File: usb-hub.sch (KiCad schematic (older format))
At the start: 51 parts, among them J1 USB_C_Receptacle_16pin, J2 USB_C_Receptacle_16pin, J3 USB_C_Receptacle_16pin, J4 Conn_01x01_Female, J5 Conn_01x01_Female, J6 Conn_01x01_Female, J7 Conn_01x01_Female, P1 CONN_02X03, Q1 PMOS, -3.6A, 0.02R, Q2 Q_NMOS_GSD 1Amp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

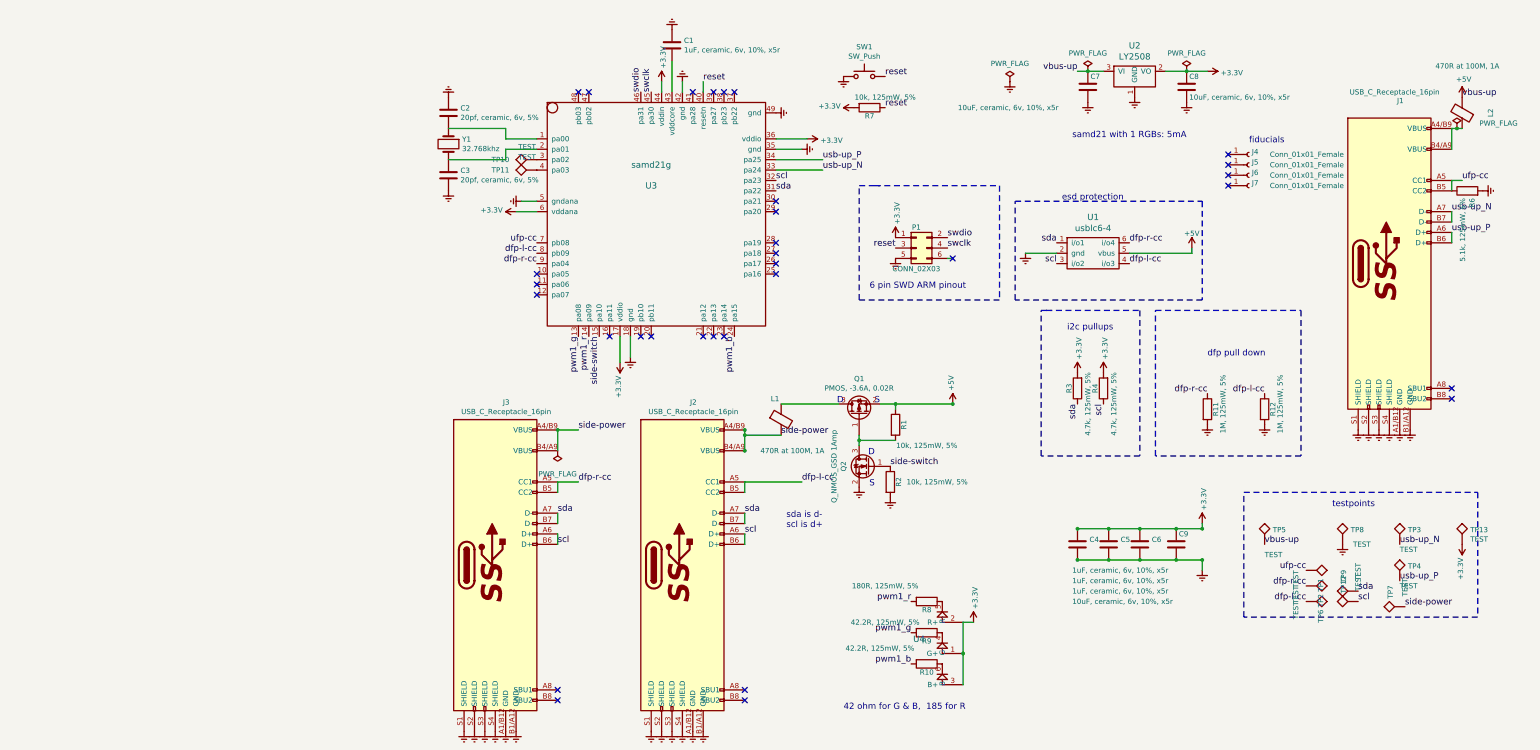
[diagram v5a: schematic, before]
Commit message: moved sockets in by 1.25mm
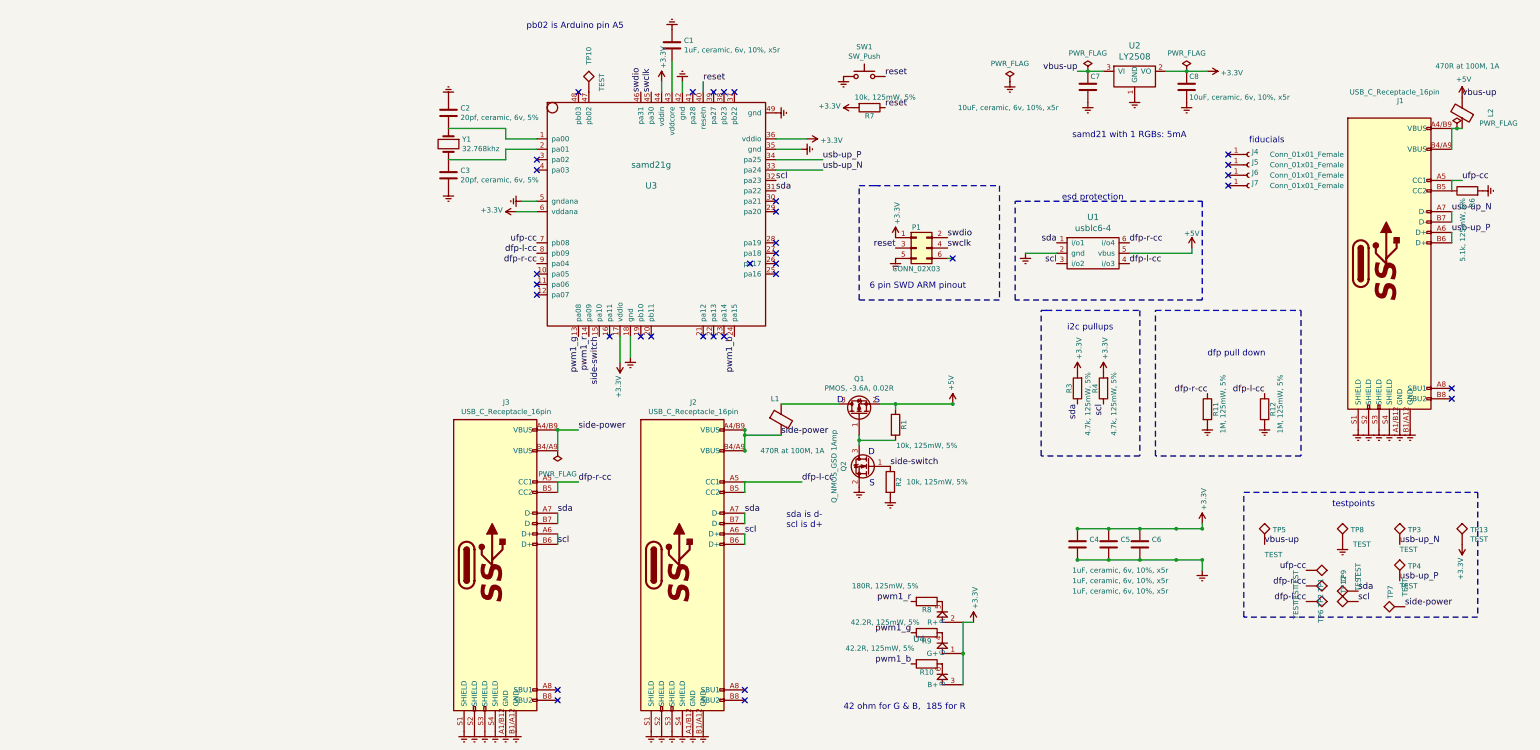
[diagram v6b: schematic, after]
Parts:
- removed C9: 10uF, ceramic, 6v, 10%, x5r, raise_fp:C_0603, symbol C
- removed TP11: TEST, raise_fp:testpoint, symbol TEST
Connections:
- net at TP10.1: now also U3.47 (pb02); no longer U3.3 (pa02)
- no-connect marks 32 -> 34
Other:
- note added: "pb02 is Arduino pin A5"
- moved on the sheet: TP10
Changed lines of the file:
@@
-$EndComp
-$Comp
-L C C9
-U 1 1 5B07FB05
-P 7900 5700
-F 0 "C9" H 7925 5800 50  0000 L CNN
-F 1 "10uF, ceramic, 6v, 10%, x5r" H 6900 5150 50  0000 L CNN
-F 2 "raise_fp:C_0603" H 7938 5550 30  0001 C CNN
-F 3 "" H 7900 5700 60  0000 C CNN
-F 4 "1288201" H 7900 5700 60  0001 C CNN "farnell #"
-F 5 "any/open" H 1900 4400 60  0001 C CNN "supplier"
-F 6 "Value" H 7900 5700 60  0001 C CNN "supplier PN"
-F 7 "Value" H 7900 5700 60  0001 C CNN "MOQ"
-F 8 "Value" H 7900 5700 60  0001 C CNN "leadtime"
-	1    7900 5700
-	1    0    0    -1
 $EndComp
 $Comp
@@
 NoConn ~ 3450 1350
 NoConn ~ 3250 1350
-NoConn ~ 2250 1350
 NoConn ~ 2150 1350
 NoConn ~ 1750 3100
@@
 L TEST TP10
 U 1 1 5B07FD09
-P 1750 2000
-F 0 "TP10" V 1750 2350 50  0000 C CNN
-F 1 "TEST" V 1874 2094 50  0000 C CNN
-F 2 "raise_fp:testpoint" H 1750 2000 50  0001 C CNN
-F 3 "" H 1750 2000 50  0001 C CNN
-F 4 "dnp" H -5550 -850 60  0001 C CNN "farnell #"
-F 5 "dnp" H -5550 -850 60  0001 C CNN "supplier"
-	1    1750 2000
-	0    -1   -1   0
-$EndComp
-$Comp
-L TEST TP11
-U 1 1 5B07FD12
-P 1750 2100
-F 0 "TP11" V 1750 2450 50  0000 C CNN
-F 1 "TEST" V 1874 2194 50  0000 C CNN
-F 2 "raise_fp:testpoint" H 1750 2100 50  0001 C CNN
-F 3 "" H 1750 2100 50  0001 C CNN
-F 4 "dnp" H -5550 -850 60  0001 C CNN "farnell #"
-F 5 "dnp" H -5550 -850 60  0001 C CNN "supplier"
-	1    1750 2100
-	0    -1   -1   0
+P 2250 1350
+F 0 "TP10" V 2250 1700 50  0000 C CNN
+F 1 "TEST" V 2374 1444 50  0000 C CNN
+F 2 "raise_fp:testpoint" H 2250 1350 50  0001 C CNN
+F 3 "" H 2250 1350 50  0001 C CNN
+F 4 "dnp" H -5050 -1500 60  0001 C CNN "farnell #"
+F 5 "dnp" H -5050 -1500 60  0001 C CNN "supplier"
+	1    2250 1350
+	1    0    0    -1
 $EndComp
 $Comp
@@
 Wire Notes Line
 	4850 2250 5050 2250
+NoConn ~ 1750 2100
+NoConn ~ 1750 2000
+NoConn ~ 3800 3000
+Text Notes 1650 750  0    60   ~ 0
+pb02 is Arduino pin A5
 $EndSCHEMATC

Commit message: replaced programming header with test pads
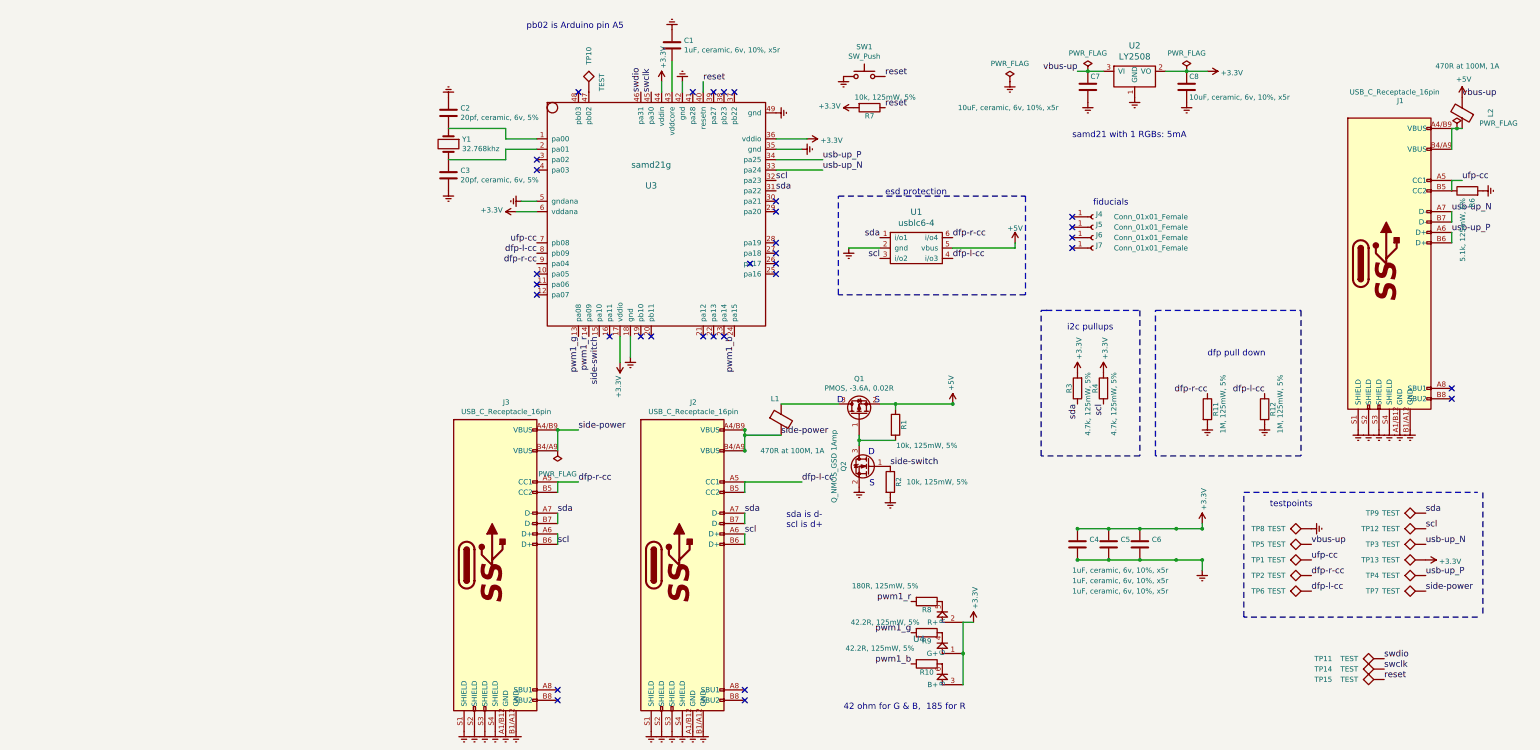
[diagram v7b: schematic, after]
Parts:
- removed P1: CONN_02X03, raise_fp:Tag-Connect_TC2030-IDC-NL, symbol Conn_02x03_Odd_Even
- added TP11, TP14, TP15: TEST, raise_fp:testpoint, symbol TEST
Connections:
- net reset: now also TP15.1
- net swclk: now also TP14.1
- net swdio: now also TP11.1
- no-connect marks 34 -> 33
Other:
- note removed: "6 pin SWD ARM pinout"
- moved on the sheet: J4, J5, J6, J7, TP1, TP12, TP13, TP2, TP3, TP4, TP5, TP6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

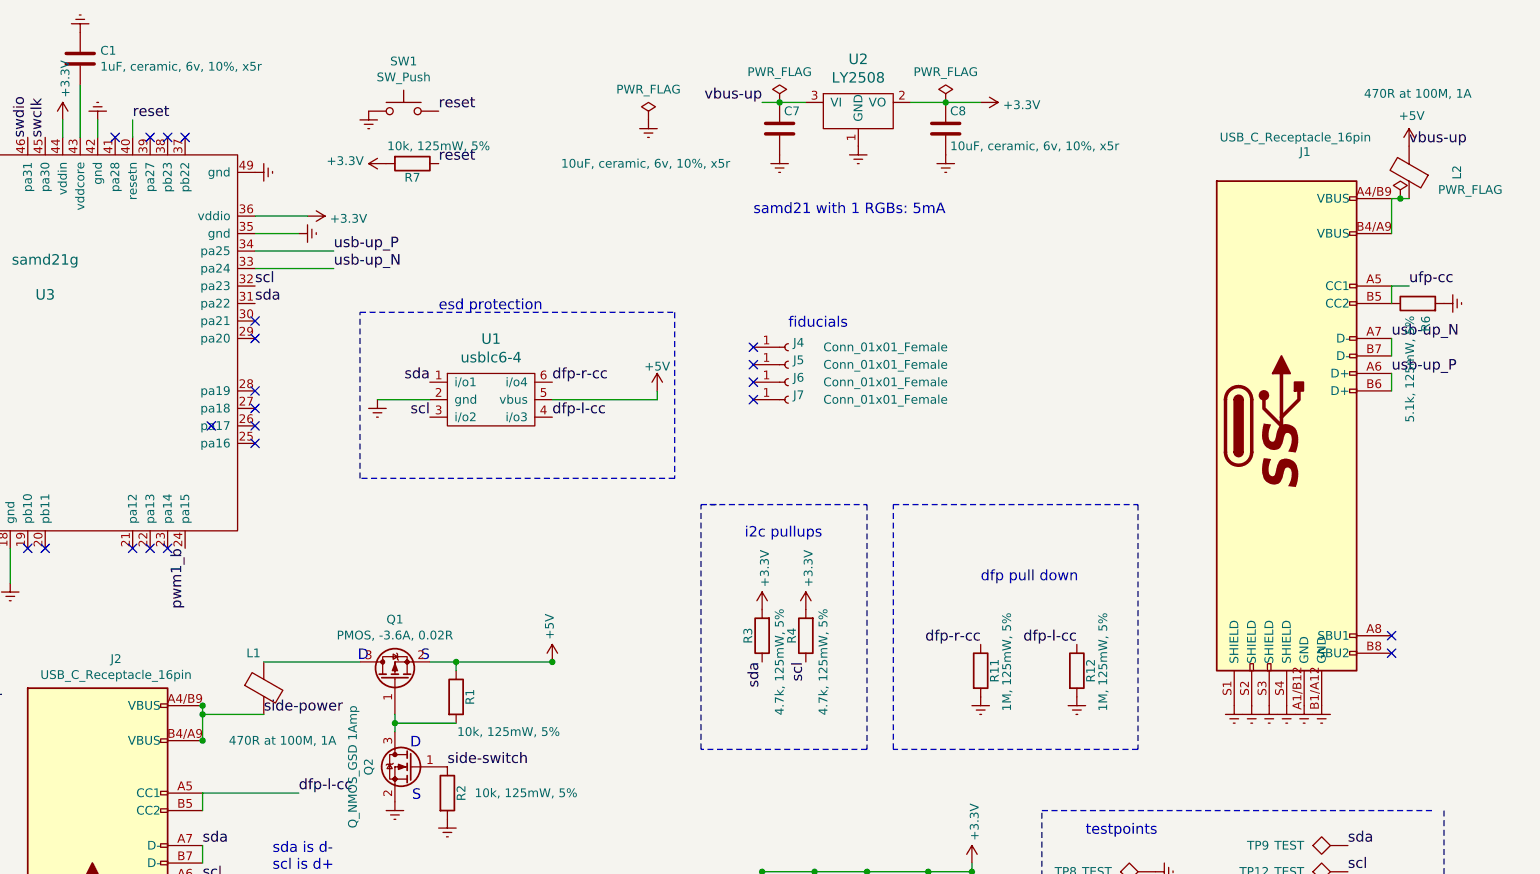
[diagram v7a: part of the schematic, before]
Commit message: dnp esd and add inductor name to component value
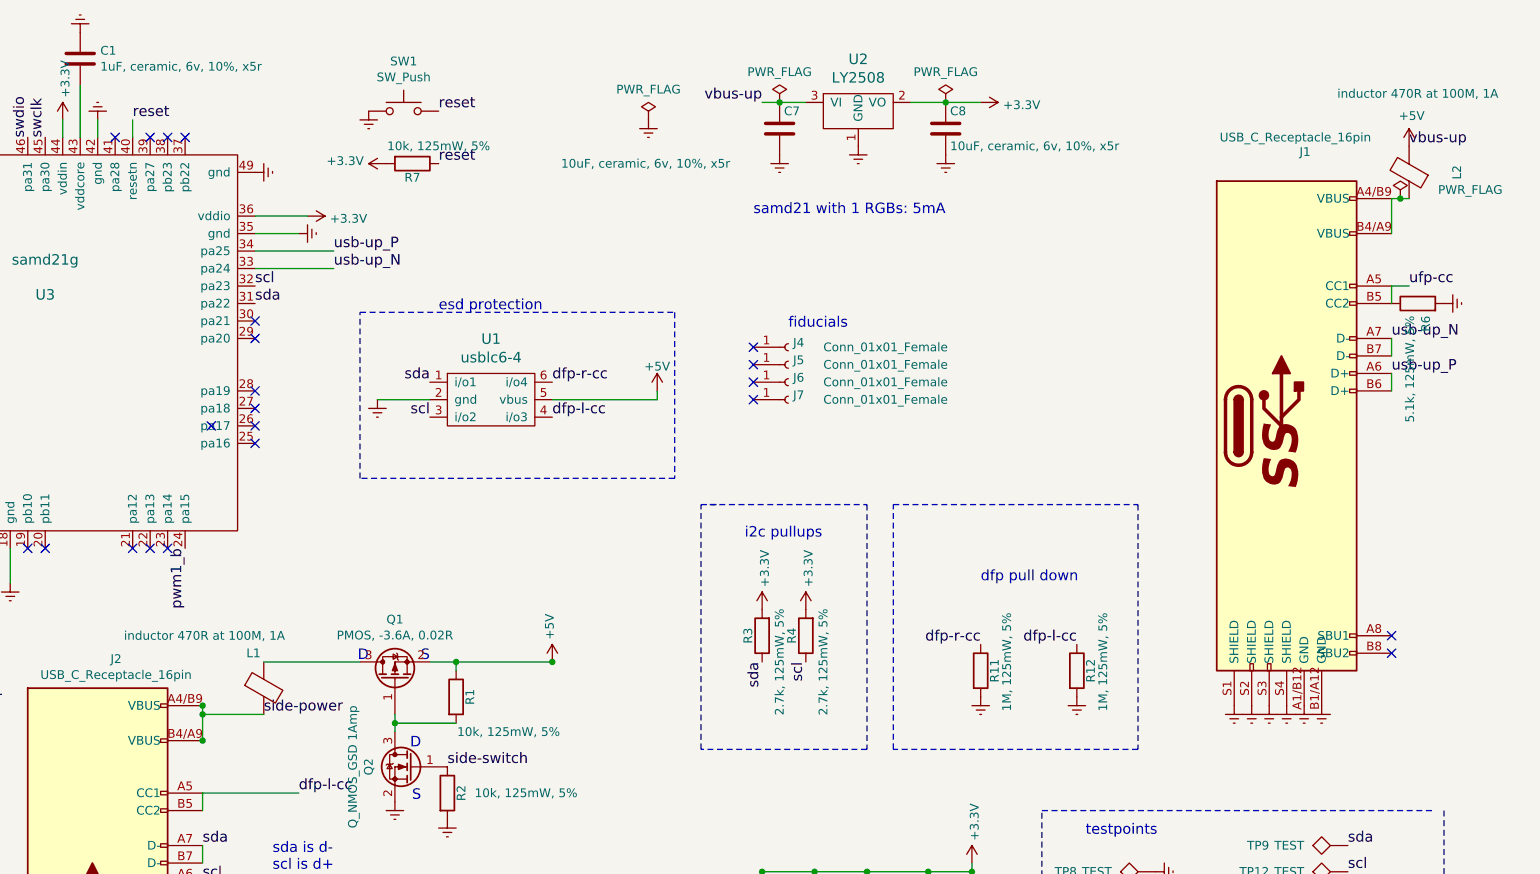
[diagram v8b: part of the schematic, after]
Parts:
- L1, L2: value 470R at 100M, 1A -> inductor 470R at 100M, 1A
- R3, R4: value 4.7k, 125mW, 5% -> 2.7k, 125mW, 5%
- U1: supplier STMicroElectronics -> dnp
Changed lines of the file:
@@
 P 10650 1550
 F 0 "L2" V 10376 1550 50  0000 C CNN
-F 1 "470R at 100M, 1A" H 10600 1100 50  0000 C CNN
+F 1 "inductor 470R at 100M, 1A" H 10600 1100 50  0000 C CNN
 F 2 "raise_fp:R_0603" V 10580 1550 50  0001 C CNN
 F 3 "" H 10650 1550 50  0001 C CNN
@@
 P 4100 4500
 F 0 "L1" H 4000 4700 50  0000 L CNN
-F 1 "470R at 100M, 1A" H 3900 4200 50  0000 L CNN
+F 1 "inductor 470R at 100M, 1A" H 3300 4800 50  0000 L CNN
 F 2 "raise_fp:R_0603" V 4030 4500 50  0001 C CNN
-F 3 "" H 4100 4500 50  0001 C CNN
+F 3 "http://www.farnell.com/datasheets/1740433.pdf?_ga=2.1215026.208533312.1536141751-2043240940.1516888894&_gac=1.12724805.1532683767.CjwKCAjwhevaBRApEiwA7aT53zTVIy1Ri4nl7qGoZV30uJtjVZm712YCRH0pjFZDdC8St9fAwf9sMBoCBakQAvD_BwE" H 4100 4500 50  0001 C CNN
 F 4 "1515745" H 4100 4500 60  0001 C CNN "farnell #"
 F 5 "Murata" H 4100 4500 60  0001 C CNN "supplier"
@@
 F 3 "" H 5400 2850 60  0001 C CNN
 F 4 "1295311" H 1200 850 60  0001 C CNN "farnell #"
-F 5 "STMicroElectronics" H 5400 2850 60  0001 C CNN "supplier"
+F 5 "dnp" H 5400 2850 60  0001 C CNN "supplier"
 F 6 "USBLC6-4SC6 " H 5400 2850 60  0001 C CNN "supplier PN"
 F 7 "Value" H 5400 2850 60  0001 C CNN "MOQ"
@@
 P 6950 4200
 F 0 "R3" V 7030 4200 50  0000 C CNN
-F 1 "4.7k, 125mW, 5%" V 6850 4350 50  0000 C CNN
+F 1 "2.7k, 125mW, 5%" V 6850 4350 50  0000 C CNN
 F 2 "raise_fp:R_0603" V 6880 4200 30  0001 C CNN
 F 3 "" H 6950 4200 30  0000 C CNN
@@
 P 7200 4200
 F 0 "R4" V 7280 4200 50  0000 C CNN
-F 1 "4.7k, 125mW, 5%" V 7100 4350 50  0000 C CNN
+F 1 "2.7k, 125mW, 5%" V 7100 4350 50  0000 C CNN
 F 2 "raise_fp:R_0603" V 7130 4200 30  0001 C CNN
 F 3 "" H 7200 4200 30  0000 C CNN
